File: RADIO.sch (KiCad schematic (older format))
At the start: 20 parts, among them U801 A7, U802 SIM_SLOT

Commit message: modified adui circuit
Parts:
- R813: manufacture (none) -> DNP
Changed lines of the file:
@@
 LIBS:mtfc8gacaeam-1m_wt
 LIBS:sn74avc2t244
-LIBS:lsm9ds1
+LIBS:WM8960CGEFL
 LIBS:3210retro-cache
 EELAYER 25 0
@@
 	12050 4000 11950 4000
 Wire Wire Line
-	11950 4300 11950 4000
+	11950 4000 11950 4300
 Wire Wire Line
 	10600 3800 10600 4300
@@
 	12050 3100 11950 3100
 Wire Wire Line
-	11950 3400 11950 3100
-Wire Wire Line
-	10550 3400 11950 3400
+	11950 3100 11950 3400
+Wire Wire Line
+	11950 3400 10550 3400
 Wire Wire Line
 	11150 3300 11150 3400
@@
 F 2 "Resistors_SMD:R_0603" V 13680 2850 50  0001 C CNN
 F 3 "" H 13750 2850 50  0000 C CNN
+F 4 "DNP" V 13750 2850 60  0000 C CNN "manufacture"
 	1    13750 2850
 	0    1    1    0

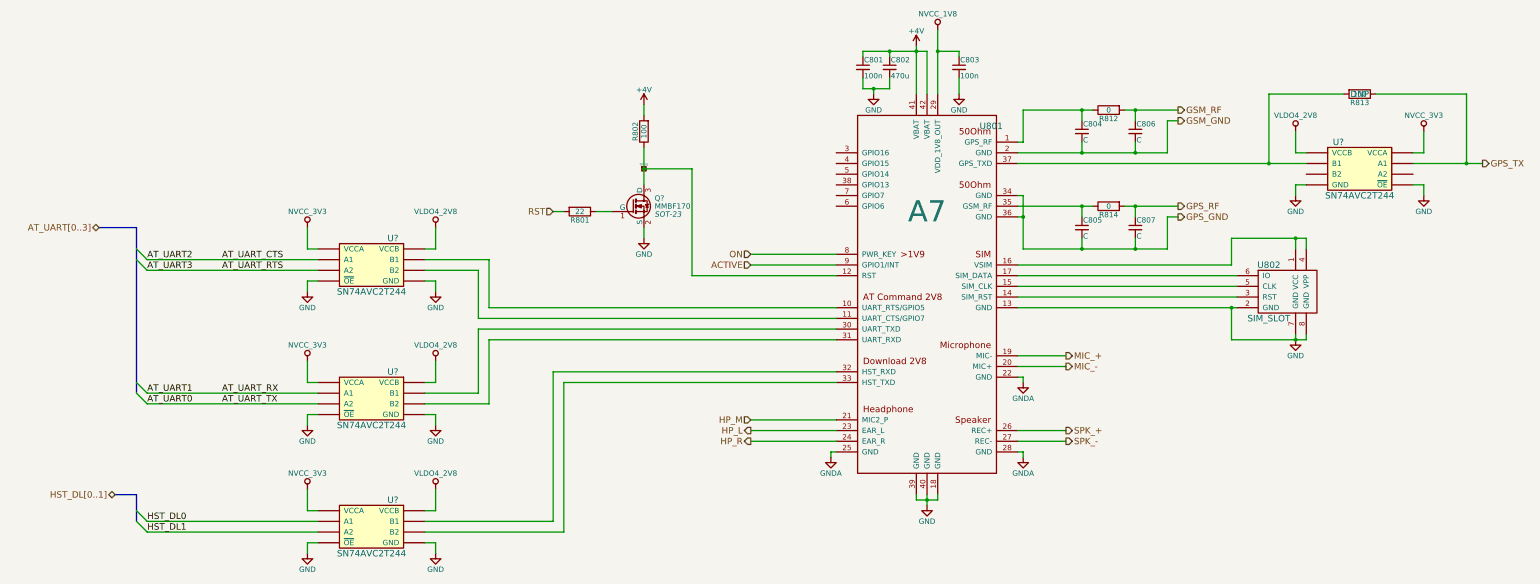
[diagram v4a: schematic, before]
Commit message: Prepare for two battery types NiMH battery for using the original battery pack LiPo battery for using long lasting modern battery
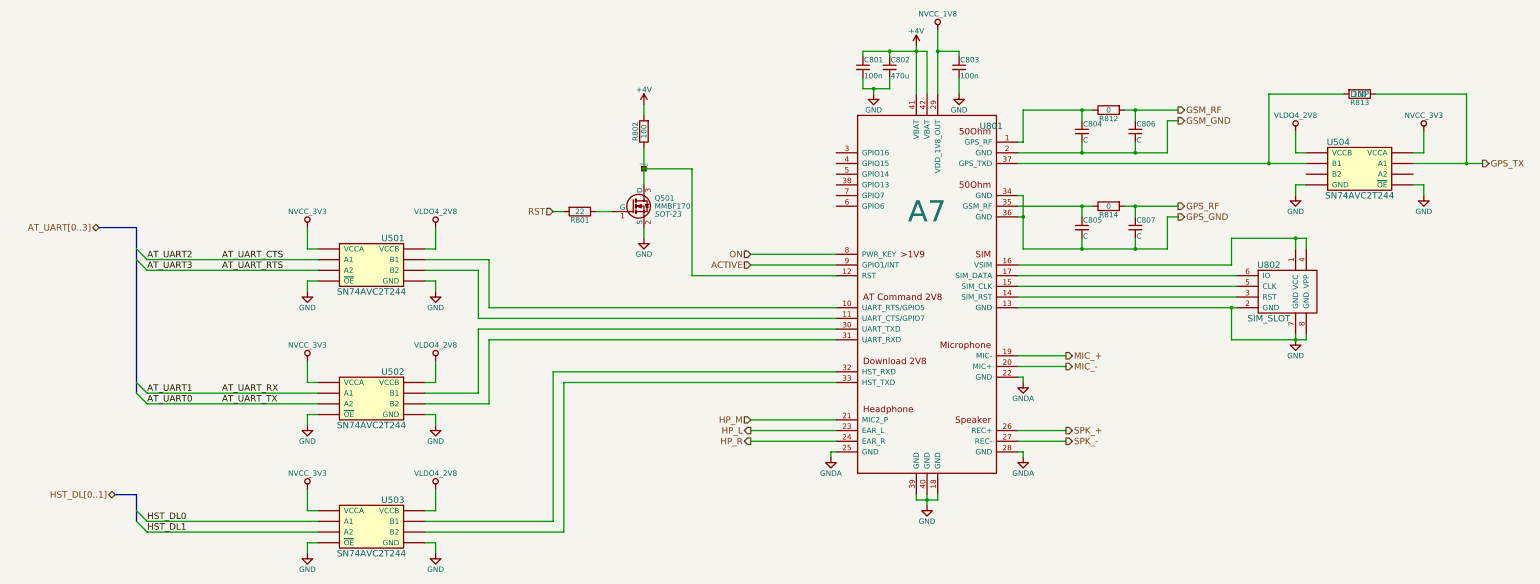
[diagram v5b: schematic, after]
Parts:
- gave numbers to parts that had none: 5
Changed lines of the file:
@@
 EESchema Schematic File Version 2
-LIBS:3210retro-rescue
-LIBS:power
-LIBS:device
-LIBS:transistors
-LIBS:conn
-LIBS:linear
-LIBS:regul
-LIBS:74xx
-LIBS:cmos4000
-LIBS:adc-dac
-LIBS:memory
-LIBS:xilinx
-LIBS:microcontrollers
-LIBS:dsp
-LIBS:microchip
-LIBS:analog_switches
-LIBS:motorola
-LIBS:texas
-LIBS:intel
-LIBS:audio
-LIBS:interface
-LIBS:digital-audio
-LIBS:philips
-LIBS:display
-LIBS:cypress
-LIBS:siliconi
-LIBS:opto
-LIBS:atmel
-LIBS:contrib
-LIBS:valves
 LIBS:a7
 LIBS:ft232rl
@@
 LIBS:sn74avc2t244
 LIBS:lsm9ds1
+LIBS:WM8960CGEFL
+LIBS:tps61021a
+LIBS:bq24400
+LIBS:power
+LIBS:device
+LIBS:transistors
+LIBS:conn
+LIBS:linear
+LIBS:regul
+LIBS:74xx
+LIBS:cmos4000
+LIBS:adc-dac
+LIBS:memory
+LIBS:xilinx
+LIBS:microcontrollers
+LIBS:dsp
+LIBS:microchip
+LIBS:analog_switches
+LIBS:motorola
+LIBS:texas
+LIBS:intel
+LIBS:audio
+LIBS:interface
+LIBS:digital-audio
+LIBS:philips
+LIBS:display
+LIBS:cypress
+LIBS:siliconi
+LIBS:opto
+LIBS:atmel
+LIBS:contrib
+LIBS:valves
 LIBS:3210retro-cache
 EELAYER 25 0
@@
 	8050 4350 8850 4350
 $Comp
-L GND #PWR072
+L GND #PWR514
 U 1 1 5805FAC7
 P 7050 4200
-F 0 "#PWR072" H 7050 3950 50  0001 C CNN
+F 0 "#PWR514" H 7050 3950 50  0001 C CNN
 F 1 "GND" H 7050 4050 50  0000 C CNN
 F 2 "" H 7050 4200 50  0000 C CNN
@@
 	7050 2950 7050 3050
 $Comp
-L +4V #PWR073
+L +4V #PWR513
 U 1 1 5805FFE4
 P 7050 2950
-F 0 "#PWR073" H 7050 2800 50  0001 C CNN
+F 0 "#PWR513" H 7050 2800 50  0001 C CNN
 F 1 "+4V" H 7050 3090 50  0000 C CNN
 F 2 "" H 7050 2950 50  0000 C CNN
@@
 GPS_TX
 $Comp
-L +4V #PWR074
+L +4V #PWR517
 U 1 1 58061BDD
 P 9600 2400
-F 0 "#PWR074" H 9600 2250 50  0001 C CNN
+F 0 "#PWR517" H 9600 2250 50  0001 C CNN
 F 1 "+4V" H 9600 2540 50  0000 C CNN
 F 2 "" H 9600 2400 50  0000 C CNN
@@
 $EndComp
 $Comp
-L GNDA #PWR075
+L GNDA #PWR515
 U 1 1 580638A9
 P 8800 6250
-F 0 "#PWR075" H 8800 6000 50  0001 C CNN
+F 0 "#PWR515" H 8800 6000 50  0001 C CNN
 F 1 "GNDA" H 8800 6100 50  0000 C CNN
 F 2 "" H 8800 6250 50  0000 C CNN
@@
 	8800 6200 8800 6250
 $Comp
-L GNDA #PWR076
+L GNDA #PWR522
 U 1 1 5806394C
 P 10600 6250
-F 0 "#PWR076" H 10600 6000 50  0001 C CNN
+F 0 "#PWR522" H 10600 6000 50  0001 C CNN
 F 1 "GNDA" H 10600 6100 50  0000 C CNN
 F 2 "" H 10600 6250 50  0000 C CNN
@@
 	10600 6200 10550 6200
 $Comp
-L GNDA #PWR077
+L GNDA #PWR521
 U 1 1 580639DF
 P 10600 5550
-F 0 "#PWR077" H 10600 5300 50  0001 C CNN
+F 0 "#PWR521" H 10600 5300 50  0001 C CNN
 F 1 "GNDA" H 10600 5400 50  0000 C CNN
 F 2 "" H 10600 5550 50  0000 C CNN
@@
 	10600 5500 10550 5500
 $Comp
-L GND #PWR078
+L GND #PWR518
 U 1 1 58063ABA
 P 9700 6700
-F 0 "#PWR078" H 9700 6450 50  0001 C CNN
+F 0 "#PWR518" H 9700 6450 50  0001 C CNN
 F 1 "GND" H 9700 6550 50  0000 C CNN
 F 2 "" H 9700 6700 50  0000 C CNN
@@
 Connection ~ 9350 2450
 $Comp
-L GND #PWR079
+L GND #PWR516
 U 1 1 5806418E
 P 9200 2850
-F 0 "#PWR079" H 9200 2600 50  0001 C CNN
+F 0 "#PWR516" H 9200 2600 50  0001 C CNN
 F 1 "GND" H 9200 2700 50  0000 C CNN
 F 2 "" H 9200 2850 50  0000 C CNN
@@
 Connection ~ 13150 5150
 $Comp
-L GND #PWR080
+L GND #PWR525
 U 1 1 58065827
 P 13150 5150
-F 0 "#PWR080" H 13150 4900 50  0001 C CNN
+F 0 "#PWR525" H 13150 4900 50  0001 C CNN
 F 1 "GND" H 13150 5000 50  0000 C CNN
 F 2 "" H 13150 5150 50  0000 C CNN
@@
 Connection ~ 9800 2450
 $Comp
-L GND #PWR082
+L GND #PWR520
 U 1 1 58065BF2
 P 10000 2850
-F 0 "#PWR082" H 10000 2600 50  0001 C CNN
+F 0 "#PWR520" H 10000 2600 50  0001 C CNN
 F 1 "GND" H 10000 2700 50  0000 C CNN
 F 2 "" H 10000 2850 50  0000 C CNN
@@
 HST_DL[0..1]
 $Comp
-L MMBF170 Q?
+L MMBF170 Q501
 U 1 1 5942BF1F
 P 6950 3900
-F 0 "Q?" H 7150 3975 50  0000 L CNN
+F 0 "Q501" H 7150 3975 50  0000 L CNN
 F 1 "MMBF170" H 7150 3900 50  0000 L CNN
 F 2 "SOT-23" H 7150 3825 50  0000 L CIN
@@
 $EndComp
 $Comp
-L SN74AVC2T244 U?
+L SN74AVC2T244 U501
 U 1 1 59464349
 P 4500 4450
-F 0 "U?" H 4700 4700 60  0000 C CNN
+F 0 "U501" H 4700 4700 60  0000 C CNN
 F 1 "SN74AVC2T244" H 4500 4200 60  0000 C CNN
 F 2 "" H 4500 4450 60  0001 C CNN
@@
 $EndComp
 $Comp
-L VLDO4_2V8 #PWR?
+L VLDO4_2V8 #PWR507
 U 1 1 594644F1
 P 5100 4100
-F 0 "#PWR?" H 5100 3950 50  0001 C CNN
+F 0 "#PWR507" H 5100 3950 50  0001 C CNN
 F 1 "VLDO4_2V8" H 5100 4250 50  0000 C CNN
 F 2 "" H 5100 4100 50  0001 C CNN
@@
 	5100 4600 5100 4700
 $Comp
-L GND #PWR?
+L GND #PWR508
 U 1 1 594649AA
 P 5100 4700
-F 0 "#PWR?" H 5100 4450 50  0001 C CNN
+F 0 "#PWR508" H 5100 4450 50  0001 C CNN
 F 1 "GND" H 5100 4550 50  0000 C CNN
 F 2 "" H 5100 4700 50  0000 C CNN
@@
 $EndComp
 $Comp
-L NVCC_3V3 #PWR?
+L NVCC_3V3 #PWR501
 U 1 1 5946648C
 P 3900 4100
-F 0 "#PWR?" H 3900 3950 50  0001 C CNN
+F 0 "#PWR501" H 3900 3950 50  0001 C CNN
 F 1 "NVCC_3V3" H 3900 4250 50  0000 C CNN
 F 2 "" H 3900 4100 50  0001 C CNN
@@
 	3900 4600 3900 4700
 $Comp
-L GND #PWR?
+L GND #PWR502
 U 1 1 5946669C
 P 3900 4700
-F 0 "#PWR?" H 3900 4450 50  0001 C CNN
+F 0 "#PWR502" H 3900 4450 50  0001 C CNN
 F 1 "GND" H 3900 4550 50  0000 C CNN
 F 2 "" H 3900 4700 50  0000 C CNN
@@
 $EndComp
 $Comp
-L SN74AVC2T244 U?
+L SN74AVC2T244 U502
 U 1 1 594667F6
 P 4500 5700
-F 0 "U?" H 4700 5950 60  0000 C CNN
+F 0 "U502" H 4700 5950 60  0000 C CNN
 F 1 "SN74AVC2T244" H 4500 5450 60  0000 C CNN
 F 2 "" H 4500 5700 60  0001 C CNN
@@
 $EndComp
 $Comp
-L VLDO4_2V8 #PWR?
+L VLDO4_2V8 #PWR509
 U 1 1 594667FC
 P 5100 5350
-F 0 "#PWR?" H 5100 5200 50  0001 C CNN
+F 0 "#PWR509" H 5100 5200 50  0001 C CNN
 F 1 "VLDO4_2V8" H 5100 5500 50  0000 C CNN
 F 2 "" H 5100 5350 50  0001 C CNN
@@
 	5100 5850 5100 5950
 $Comp
-L GND #PWR?
+L GND #PWR510
 U 1 1 59466808
 P 5100 5950
-F 0 "#PWR?" H 5100 5700 50  0001 C CNN
+F 0 "#PWR510" H 5100 5700 50  0001 C CNN
 F 1 "GND" H 5100 5800 50  0000 C CNN
 F 2 "" H 5100 5950 50  0000 C CNN
@@
 $EndComp
 $Comp
-L NVCC_3V3 #PWR?
+L NVCC_3V3 #PWR503
 U 1 1 5946680E
 P 3900 5350
-F 0 "#PWR?" H 3900 5200 50  0001 C CNN
+F 0 "#PWR503" H 3900 5200 50  0001 C CNN
 F 1 "NVCC_3V3" H 3900 5500 50  0000 C CNN
 F 2 "" H 3900 5350 50  0001 C CNN
@@
 	3900 5850 3900 5950
 $Comp
-L GND #PWR?
+L GND #PWR504
 U 1 1 5946681A
 P 3900 5950
-F 0 "#PWR?" H 3900 5700 50  0001 C CNN
+F 0 "#PWR504" H 3900 5700 50  0001 C CNN
 F 1 "GND" H 3900 5800 50  0000 C CNN
 F 2 "" H 3900 5950 50  0000 C CNN
@@
 AT_UART_TX
 $Comp
-L SN74AVC2T244 U?
+L SN74AVC2T244 U503
 U 1 1 594A7415
 P 4500 6900
-F 0 "U?" H 4700 7150 60  0000 C CNN
+F 0 "U503" H 4700 7150 60  0000 C CNN
 F 1 "SN74AVC2T244" H 4500 6650 60  0000 C CNN
 F 2 "" H 4500 6900 60  0001 C CNN
@@
 $EndComp
 $Comp
-L VLDO4_2V8 #PWR?
+L VLDO4_2V8 #PWR511
 U 1 1 594A741B
 P 5100 6550
-F 0 "#PWR?" H 5100 6400 50  0001 C CNN
+F 0 "#PWR511" H 5100 6400 50  0001 C CNN
 F 1 "VLDO4_2V8" H 5100 6700 50  0000 C CNN
 F 2 "" H 5100 6550 50  0001 C CNN
@@
 	5100 7050 5100 7150
 $Comp
-L GND #PWR?
+L GND #PWR512
 U 1 1 594A7427
 P 5100 7150
-F 0 "#PWR?" H 5100 6900 50  0001 C CNN
+F 0 "#PWR512" H 5100 6900 50  0001 C CNN
 F 1 "GND" H 5100 7000 50  0000 C CNN
 F 2 "" H 5100 7150 50  0000 C CNN
@@
 $EndComp
 $Comp
-L NVCC_3V3 #PWR?
+L NVCC_3V3 #PWR505
 U 1 1 594A742D
 P 3900 6550
-F 0 "#PWR?" H 3900 6400 50  0001 C CNN
+F 0 "#PWR505" H 3900 6400 50  0001 C CNN
 F 1 "NVCC_3V3" H 3900 6700 50  0000 C CNN
 F 2 "" H 3900 6550 50  0001 C CNN
@@
 	3900 7050 3900 7150
 $Comp
-L GND #PWR?
+L GND #PWR506
 U 1 1 594A7439
 P 3900 7150
-F 0 "#PWR?" H 3900 6900 50  0001 C CNN
+F 0 "#PWR506" H 3900 6900 50  0001 C CNN
 F 1 "GND" H 3900 7000 50  0000 C CNN
 F 2 "" H 3900 7150 50  0000 C CNN
@@
 	6300 5550 8850 5550
 $Comp
-L SN74AVC2T244 U?
+L SN74AVC2T244 U504
 U 1 1 594A9232
 P 13750 3550
-F 0 "U?" H 13950 3800 60  0000 C CNN
+F 0 "U504" H 13950 3800 60  0000 C CNN
 F 1 "SN74AVC2T244" H 13750 3300 60  0000 C CNN
 F 2 "" H 13750 3550 60  0001 C CNN
@@
 $EndComp
 $Comp
-L VLDO4_2V8 #PWR?
+L VLDO4_2V8 #PWR523
 U 1 1 594A9238
 P 13150 3200
-F 0 "#PWR?" H 13150 3050 50  0001 C CNN
+F 0 "#PWR523" H 13150 3050 50  0001 C CNN
 F 1 "VLDO4_2V8" H 13150 3350 50  0000 C CNN
 F 2 "" H 13150 3200 50  0001 C CNN
@@
 	13150 3700 13150 3800
 $Comp
-L GND #PWR?
+L GND #PWR524
 U 1 1 594A9244
 P 13150 3800
-F 0 "#PWR?" H 13150 3550 50  0001 C CNN
+F 0 "#PWR524" H 13150 3550 50  0001 C CNN
 F 1 "GND" H 13150 3650 50  0000 C CNN
 F 2 "" H 13150 3800 50  0000 C CNN
@@
 $EndComp
 $Comp
-L NVCC_3V3 #PWR?
+L NVCC_3V3 #PWR526
 U 1 1 594A924A
 P 14350 3200
-F 0 "#PWR?" H 14350 3050 50  0001 C CNN
+F 0 "#PWR526" H 14350 3050 50  0001 C CNN
 F 1 "NVCC_3V3" H 14350 3350 50  0000 C CNN
 F 2 "" H 14350 3200 50  0001 C CNN
@@
 	14350 3700 14350 3800
 $Comp
-L GND #PWR?
+L GND #PWR527
 U 1 1 594A9254
 P 14350 3800
-F 0 "#PWR?" H 14350 3550 50  0001 C CNN
+F 0 "#PWR527" H 14350 3550 50  0001 C CNN
 F 1 "GND" H 14350 3650 50  0000 C CNN
 F 2 "" H 14350 3800 50  0000 C CNN
@@
 	10600 4300 11950 4300
 $Comp
-L NVCC_1V8 #PWR?
+L NVCC_1V8 #PWR519
 U 1 1 594AAC99
 P 9800 2250
-F 0 "#PWR?" H 9800 2100 50  0001 C CNN
+F 0 "#PWR519" H 9800 2100 50  0001 C CNN
 F 1 "NVCC_1V8" H 9800 2400 50  0000 C CNN
 F 2 "" H 9800 2250 50  0001 C CNN

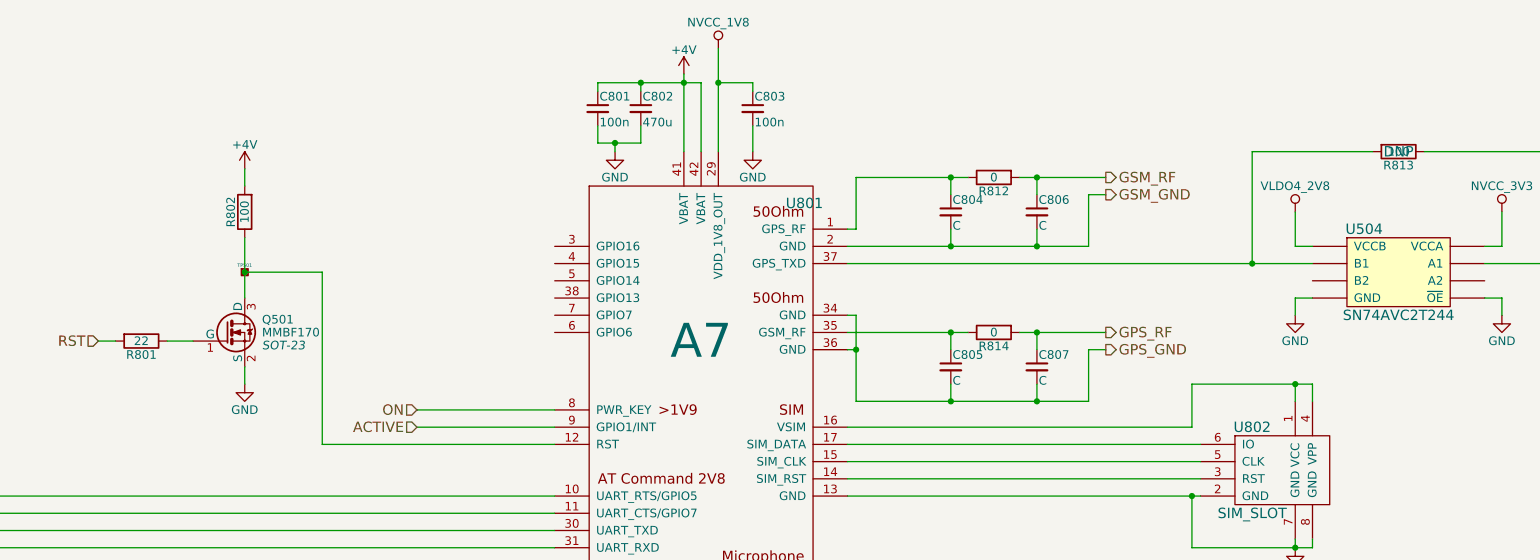
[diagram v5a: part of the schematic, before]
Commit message: Changed several voltage rail connections Removed non existing rails Added circuit for NiMH charging
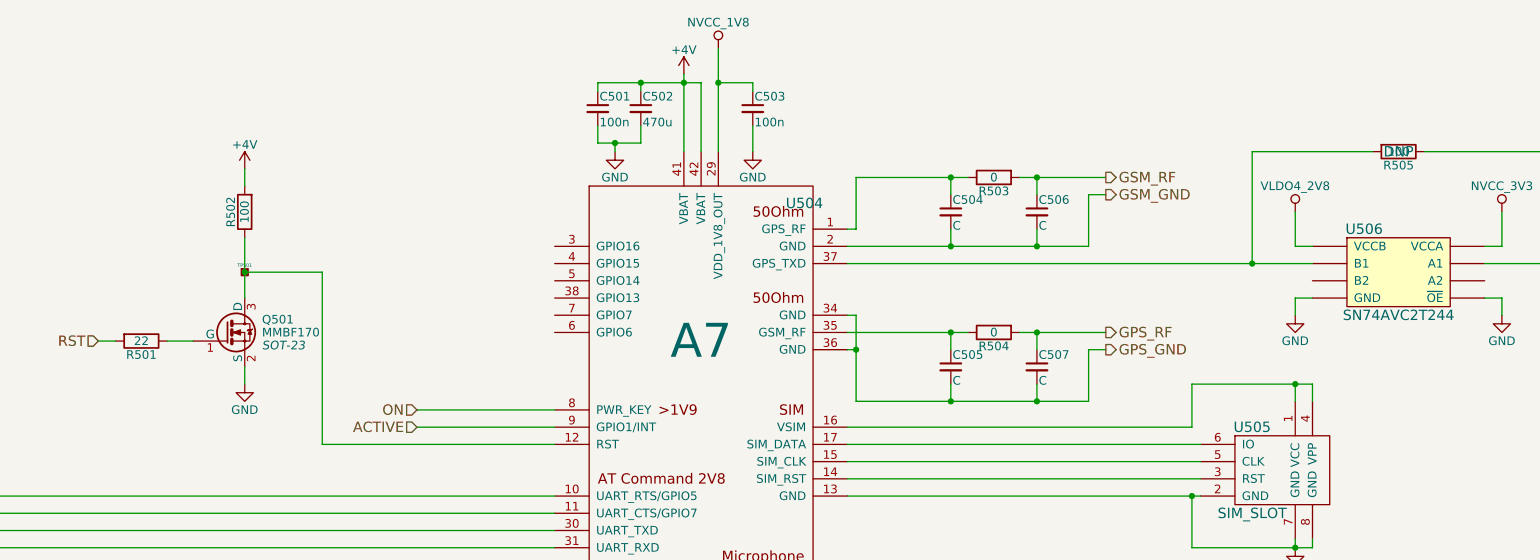
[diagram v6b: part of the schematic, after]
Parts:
- renumbered C801 to C501, C802 to C502, C803 to C503, C804 to C504, C805 to C505, C806 to C506, C807 to C507, R801 to R501, R802 to R502, R812 to R503, R814 to R504, R813 to R505, U801 to U504, U802 to U505, U504 to U506
